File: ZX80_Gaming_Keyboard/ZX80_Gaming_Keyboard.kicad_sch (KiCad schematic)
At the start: 52 parts, among them J1 KB1, J2 KB2, J3 0_SPACE, SW1 1, SW10 0, SW11 Q, SW12 W, SW13 E, SW14 R, SW15 T, SW16 Y, SW17 U, SW18 I, SW19 O, SW2 2, SW20 P, SW21 A, SW22 S, SW23 D, SW24 F, SW25 G, SW26 H, SW27 J, SW28 K, SW29 L, SW3 3, SW30 NL, SW31 SHIFT, SW32 Z, SW33 X, SW34 C, SW35 V, SW36 B, SW37 N, SW38 M, SW39 DOT, SW4 4, SW40 SPACE, SW41 LEFT, SW42 DOWN, SW43 UP, SW44 RIGHT, SW45 RUBOUT, SW5 5, SW6 6, SW7 7, SW8 8, SW9 9

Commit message: Finalised keyboard design for testing
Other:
- note added: "Switch [SPACE] bar to [0] (jump key in ZX80 KONG)"
- note removed: "Switch [SPACE] bar to [0]"
- company: (none) -> Brett Hallen
- title: (none) -> ZX80 Gaming Keyboard
- moved on the sheet: SW41, SW42, SW43, SW44
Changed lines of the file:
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@@
 	(generator_version "9.0")
 	(paper "A4")
-	(text "Switch [SPACE] bar to [0]"
+	(title_block
+		(title "ZX80 Gaming Keyboard")
+		(date "22-May-2025")
+		(rev "A")
+		(company "Brett Hallen")
+		(comment 1 "www.youtube.com/@Brfff")
+	)
+	(text "Switch [SPACE] bar to [0]\n(jump key in ZX80 KONG)"
 		(exclude_from_sim no)
 		(at 237.49 149.86 0)
@@
 		)
 	)
+	(text_box "Dedicated [DELETE] key\n[SHIFT] + [0]"
+		(exclude_from_sim no)
+		(at 199.39 20.32 0)
+		(size 38.1 29.21)
+		(margins 0.9525 0.9525 0.9525 0.9525)
+		(stroke
+			(width 0)
+			(type solid)
+		)
+		(fill
+			(type none)
+		)
+		(effects
+			(font
+				(size 1.27 1.27)
+			)
+			(justify left top)
+		)
+	)
+	(text_box "Dedicated cursor keys\n[5], [6], [7], [8]"
+		(exclude_from_sim no)
+		(at 81.28 19.05 0)
+		(size 86.36 25.4)
+		(margins 0.9525 0.9525 0.9525 0.9525)
+		(stroke
+			(width 0)
+			(type solid)
+		)
+		(fill
+			(type none)
+		)
+		(effects
+			(font
+				(size 1.27 1.27)
+			)
+			(justify left top)
+		)
+	)
 	(junction
 		(at 234.95 118.11)
@@
 	)
 	(junction
-		(at 171.45 39.37)
+		(at 138.43 39.37)
 		(diameter 0)
 		(color 0 0 0 0)
@@
 	(wire
 		(pts
-			(xy 171.45 39.37) (xy 186.69 39.37)
+			(xy 138.43 39.37) (xy 153.67 39.37)
 		)
 		(stroke
@@
 	(wire
 		(pts
-			(xy 153.67 39.37) (xy 171.45 39.37)
+			(xy 120.65 39.37) (xy 138.43 39.37)
 		)
 		(stroke
@@
 	(global_label "A11"
 		(shape input)
-		(at 135.89 41.91 0)
+		(at 101.6 40.64 0)
 		(fields_autoplaced yes)
 		(effects
@@
 		)
 		(property "Intersheetrefs" "${INTERSHEET_REFS}"
-			(at 142.3828 41.91 0)
+			(at 108.0928 40.64 0)
 			(effects
 				(font
@@
 	(global_label "COL2"
 		(shape input)
-		(at 166.37 34.29 180)
+		(at 133.35 34.29 180)
 		(fields_autoplaced yes)
 		(effects
@@
 		)
 		(property "Intersheetrefs" "${INTERSHEET_REFS}"
-			(at 158.5467 34.29 0)
+			(at 125.5267 34.29 0)
 			(effects
 				(font
@@
 	(global_label "COL3"
 		(shape input)
-		(at 181.61 34.29 180)
+		(at 148.59 34.29 180)
 		(fields_autoplaced yes)
 		(effects
@@
 		)
 		(property "Intersheetrefs" "${INTERSHEET_REFS}"
-			(at 173.7867 34.29 0)
+			(at 140.7667 34.29 0)
 			(effects
 				(font
@@
 	(global_label "COL1"
 		(shape input)
-		(at 148.59 34.29 180)
+		(at 115.57 34.29 180)
 		(fields_autoplaced yes)
 		(effects
@@
 		)
 		(property "Intersheetrefs" "${INTERSHEET_REFS}"
-			(at 140.7667 34.29 0)
+			(at 107.7467 34.29 0)
 			(effects
 				(font
@@
 	(global_label "A12"
 		(shape input)
-		(at 186.69 39.37 0)
+		(at 153.67 39.37 0)
 		(fields_autoplaced yes)
 		(effects
@@
 		)
 		(property "Intersheetrefs" "${INTERSHEET_REFS}"
-			(at 193.1828 39.37 0)
+			(at 160.1628 39.37 0)
 			(effects
 				(font
@@
 	(global_label "COL1"
 		(shape input)
-		(at 130.81 36.83 180)
+		(at 96.52 35.56 180)
 		(fields_autoplaced yes)
 		(effects
@@
 		)
 		(property "Intersheetrefs" "${INTERSHEET_REFS}"
-			(at 122.9867 36.83 0)
+			(at 88.6967 35.56 0)
 			(effects
 				(font
@@
 	(symbol
 		(lib_id "Switch:SW_Push_45deg")
-		(at 168.91 36.83 0)
+		(at 135.89 36.83 0)
 		(unit 1)
 		(exclude_from_sim no)
@@
 		(fields_autoplaced yes)
 		(property "Reference" "SW43"
-			(at 168.91 29.21 0)
+			(at 135.89 29.21 0)
 			(effects
 				(font
@@
 		)
 		(property "Value" "UP"
-			(at 168.91 31.75 0)
+			(at 135.89 31.75 0)
 			(effects
 				(font
@@
 		)
 		(property "Footprint" "Button_Switch_Keyboard:SW_Cherry_MX_1.00u_PCB"
-			(at 168.91 36.83 0)
+			(at 135.89 36.83 0)
 			(effects
 				(font
@@
 		)
 		(property "Datasheet" "~"
-			(at 168.91 36.83 0)
+			(at 135.89 36.83 0)
 			(effects
 				(font
@@
 		)
 		(property "Description" "Push button switch, normally open, two pins, 45° tilted"
-			(at 168.91 36.83 0)
+			(at 135.89 36.83 0)
 			(effects
 				(font
@@
 	(symbol
 		(lib_id "Switch:SW_Push_45deg")
-		(at 133.35 39.37 0)
+		(at 99.06 38.1 0)
 		(unit 1)
 		(exclude_from_sim no)
@@
 		(fields_autoplaced yes)
 		(property "Reference" "SW41"
-			(at 133.35 31.75 0)
+			(at 99.06 30.48 0)
 			(effects
 				(font
@@
 		)
 		(property "Value" "LEFT"
-			(at 133.35 34.29 0)
+			(at 99.06 33.02 0)
 			(effects
 				(font
@@
 		)
 		(property "Footprint" "Button_Switch_Keyboard:SW_Cherry_MX_1.00u_PCB"
-			(at 133.35 39.37 0)
+			(at 99.06 38.1 0)
 			(effects
 				(font
@@
 		)
 		(property "Datasheet" "~"
-			(at 133.35 39.37 0)
+			(at 99.06 38.1 0)
 			(effects
 				(font
@@
 		)
 		(property "Description" "Push button switch, normally open, two pins, 45° tilted"
-			(at 133.35 39.37 0)
+			(at 99.06 38.1 0)
 			(effects
 				(font
@@
 	(symbol
 		(lib_id "Switch:SW_Push_45deg")
-		(at 184.15 36.83 0)
+		(at 151.13 36.83 0)
 		(unit 1)
 		(exclude_from_sim no)
@@
 		(fields_autoplaced yes)
 		(property "Reference" "SW44"
-			(at 184.15 29.21 0)
+			(at 151.13 29.21 0)
 			(effects
 				(font
@@
 		)
 		(property "Value" "RIGHT"
-			(at 184.15 31.75 0)
+			(at 151.13 31.75 0)
 			(effects
 				(font
@@
 		)
 		(property "Footprint" "Button_Switch_Keyboard:SW_Cherry_MX_1.00u_PCB"
-			(at 184.15 36.83 0)
+			(at 151.13 36.83 0)
 			(effects
 				(font
@@
 		)
 		(property "Datasheet" "~"
-			(at 184.15 36.83 0)
+			(at 151.13 36.83 0)
 			(effects
 				(font
@@
 		)
 		(property "Description" "Push button switch, normally open, two pins, 45° tilted"
-			(at 184.15 36.83 0)
+			(at 151.13 36.83 0)
 			(effects
 				(font
@@
 	(symbol
 		(lib_id "Switch:SW_Push_45deg")
-		(at 151.13 36.83 0)
+		(at 118.11 36.83 0)
 		(unit 1)
 		(exclude_from_sim no)
@@
 		(fields_autoplaced yes)
 		(property "Reference" "SW42"
-			(at 151.13 29.21 0)
+			(at 118.11 29.21 0)
 			(effects
 				(font
@@
 		)
 		(property "Value" "DOWN"
-			(at 151.13 31.75 0)
+			(at 118.11 31.75 0)
 			(effects
 				(font
@@
 		)
 		(property "Footprint" "Button_Switch_Keyboard:SW_Cherry_MX_1.00u_PCB"
-			(at 151.13 36.83 0)
+			(at 118.11 36.83 0)
 			(effects
 				(font
@@
 		)
 		(property "Datasheet" "~"
-			(at 151.13 36.83 0)
+			(at 118.11 36.83 0)
 			(effects
 				(font
@@
 		)
 		(property "Description" "Push button switch, normally open, two pins, 45° tilted"
-			(at 151.13 36.83 0)
+			(at 118.11 36.83 0)
 			(effects
 				(font

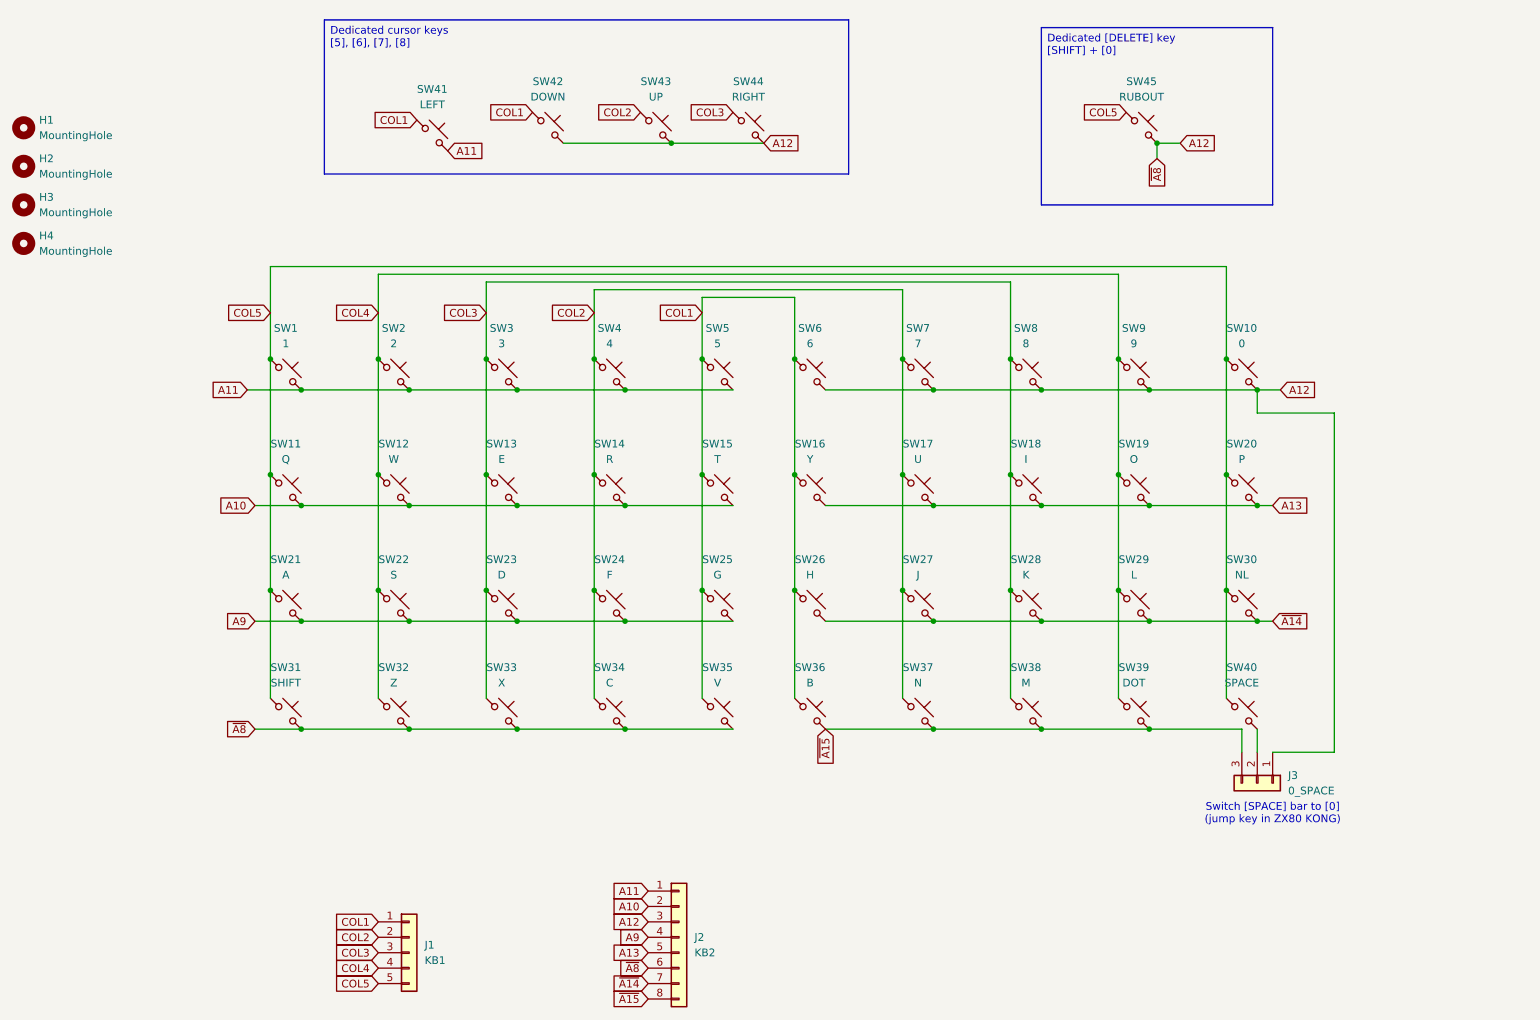
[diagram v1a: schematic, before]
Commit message: Revised PCB layout correcting errors
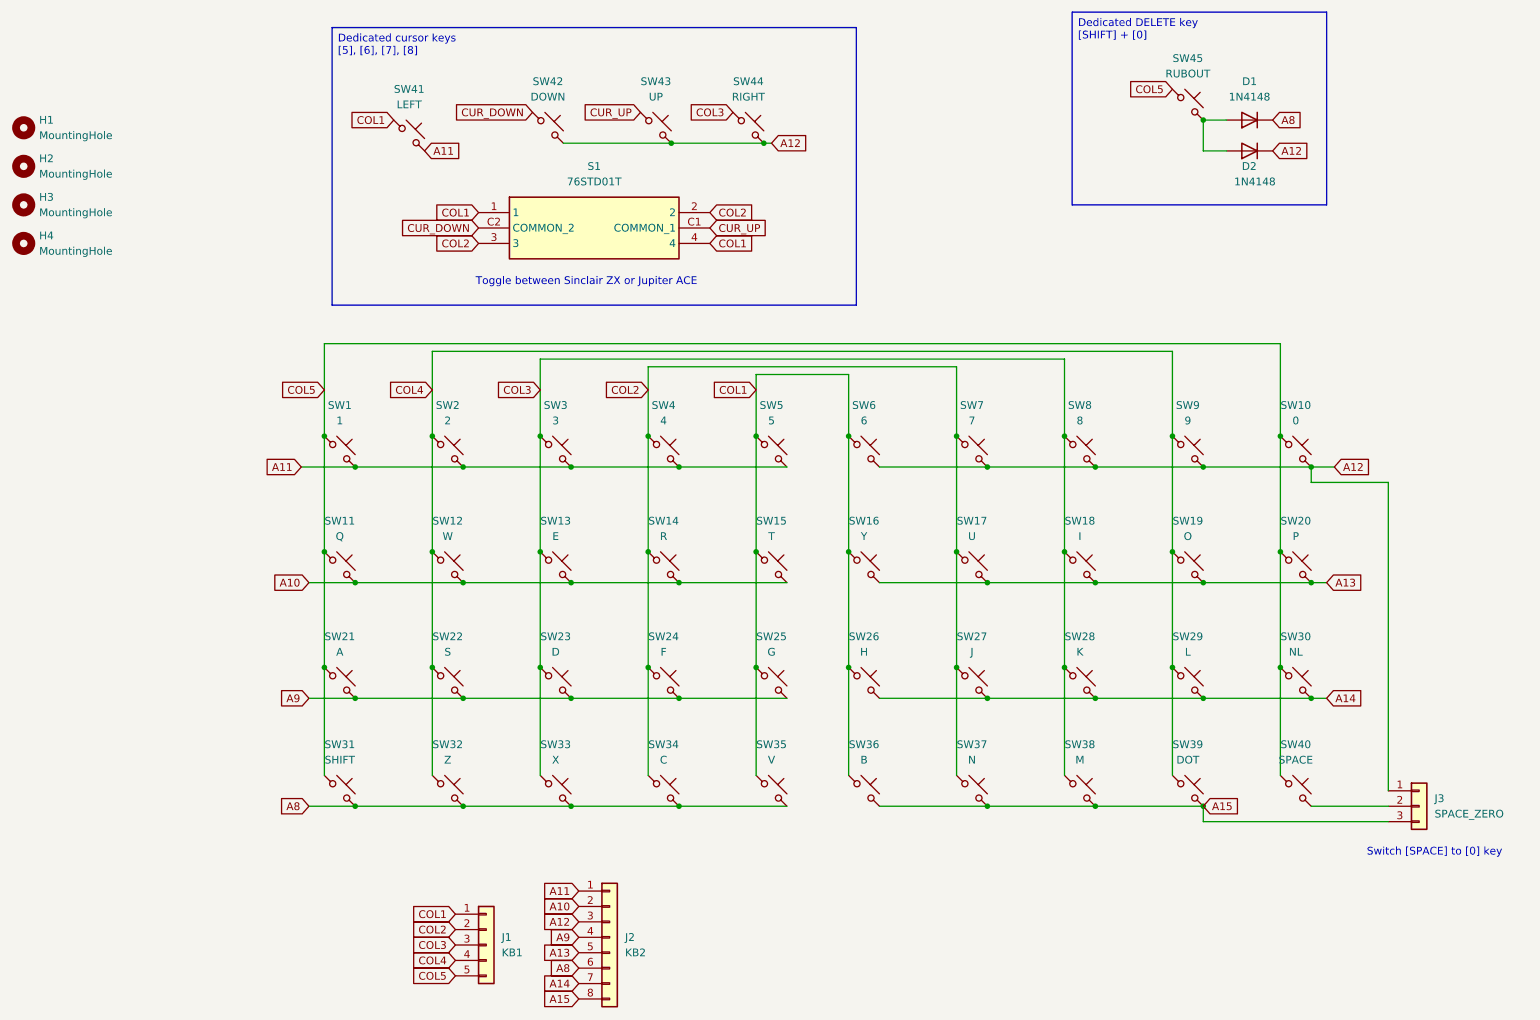
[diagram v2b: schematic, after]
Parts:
- added D1, D2: 1N4148, Diode_THT:D_DO-35_SOD27_P7.62mm_Horizontal, symbol Device:D
- added S1: 76STD01T, Button_Switch_THT:76STD01T, symbol Switch:76STD01T
- J3: value 0_SPACE -> SPACE_ZERO
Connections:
- net A12: now also D2.1 (K); no longer J2.6 (Pin_6), SW31.2, SW32.2, SW33.2, SW34.2, SW35.2, SW45.2
- net COL1: now also S1.1, S1.4; no longer SW42.1
- net COL2: now also S1.2, S1.3; no longer SW43.1
- net ~{A14} renamed A14
- net ~{A15} renamed A15
- new net: D1.2 (A), D2.2 (A), SW45.2
- new net A8: D1.1 (K), J2.6 (Pin_6), SW31.2, SW32.2, SW33.2, SW34.2, SW35.2
- new net CUR_DOWN: S1.C2 (COMMON_2), SW42.1
- new net CUR_UP: S1.C1 (COMMON_1), SW43.1
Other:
- note added: "Switch [SPACE] to [0] key"
- note added: "Toggle between Sinclair ZX or Jupiter ACE"
- note removed: "Switch [SPACE] bar to [0] (jump key in ZX80 KONG)"
- moved on the sheet: J1, J2, SW1, SW10, SW11, SW12, SW13, SW14, SW15, SW16, SW17, SW18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
